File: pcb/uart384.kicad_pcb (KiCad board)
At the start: 2 copper layers, 54.1 x 23.5 mm, 42 parts, among them IC1 ICE40LP384-SG32, J1 USB_A, J2 TC2050, J3 TC2050_ext, J4 Conn_02x07_Odd_Even, SW1 SW_Push, U1 AT25DF256-SSHN, U2 CP2102-QFN28, U3 MIC5365-1.2YC5, U4 AMS1117-2.5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

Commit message: plaster everything with licenses and copyright notices.
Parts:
- added REF**: OSHW-Logo2_7.3x6mm_SilkScreen, Symbol:OSHW-Logo2_7.3x6mm_SilkScreen, F.Cu at (112.9, 75.1)
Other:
- board text added: "CERN-OHL-W v2"
- board text added: "This item was designed by an implementation of RFC2795. Please send fruit to the designer. No bananas."
- board text added: "by dpiegdon"
- board text added: "v2.0~ UART384"
- board text removed: "UART384"
- board text removed: "v2.0~ by dpiegdon"

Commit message: optimize the shit out of the PCB because I'm bored.
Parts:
- JP2: renamed from JP1; footprint Jumper:SolderJumper-3_P1.3mm_Bridged2Bar12_RoundedPad1.0x1.5mm -> Jumper:SolderJumper-3_P1.3mm_Open_RoundedPad1.0x1.5mm
- moved D3 13.3 mm to (101.5, 84.7), turned to -90 degrees
- moved C9 3.11 mm to (105.1, 83.6), turned to -90 degrees
- moved U3 2.34 mm to (107.6, 85.2), turned to 180 degrees
- moved C5 1.91 mm to (107.5, 82.9), turned to 0 degrees
- moved C6 1.90 mm to (104.2, 86.0)
- moved C7 1.89 mm to (98.2, 73.0), turned to 180 degrees
- moved C1 1.68 mm to (99.2, 71.5), turned to 180 degrees
- moved Y1 1.06 mm to (110.8, 84.5)
- moved C13 1.06 mm to (103.4, 83.6), turned to 90 degrees
- moved C4 0.64 mm to (97.2, 74.7), turned to 180 degrees
- renumbered JP2 to JP1
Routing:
- net GND: track 98.3 -> 115.8 mm, vias 7 -> 10
- net +2V5: track 11.1 -> 8.44 mm, vias 2 -> 1
- net +1V2: track 9.04 -> 11.5 mm
- net /CLK: track 7.30 -> 8.01 mm
- net /UART_CTS: track 9.09 -> 8.52 mm
- net +3V3: track 62.5 -> 62.6 mm, vias 20 -> 19

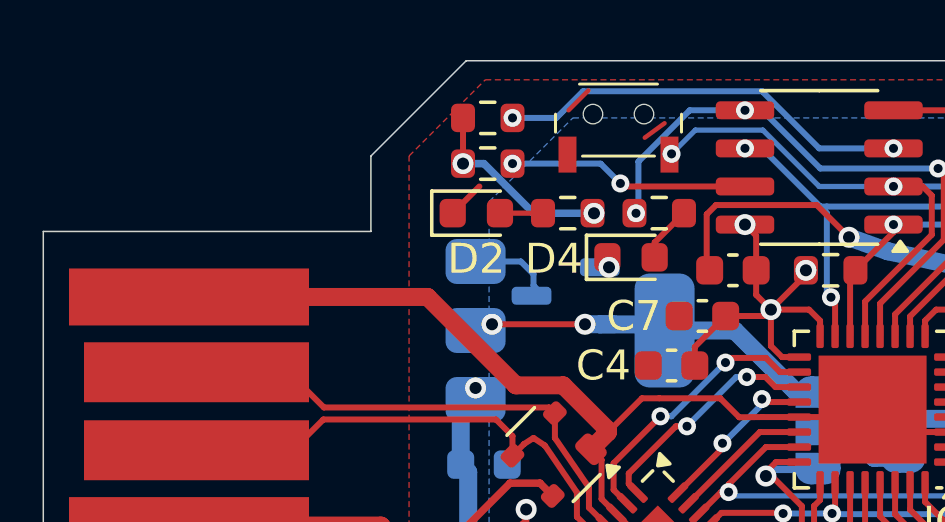
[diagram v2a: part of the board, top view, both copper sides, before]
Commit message: PCB: add in-line resistor to switch SW1 to avoid possible shorts.
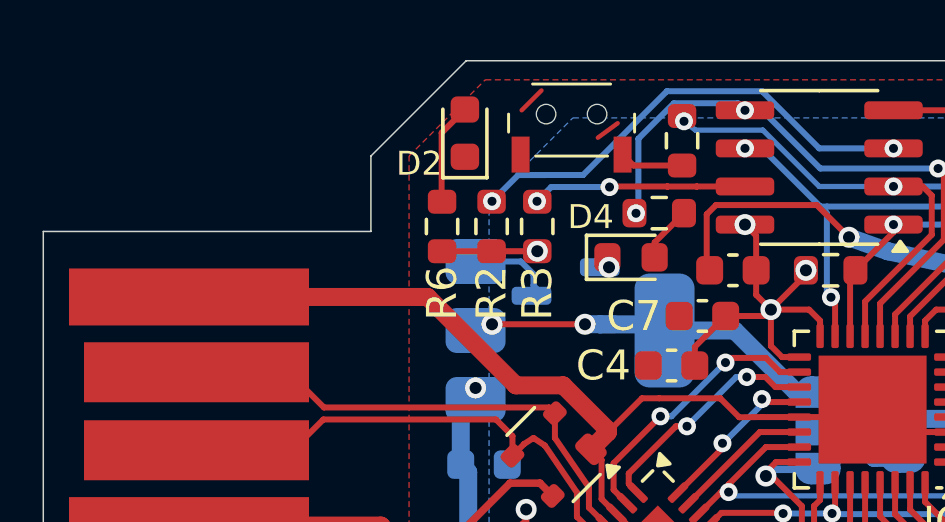
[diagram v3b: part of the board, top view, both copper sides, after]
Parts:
- added R8: 4k7, Resistor_SMD:R_0603_1608Metric, F.Cu at (97.5, 67.2)
- moved R6 4.21 mm to (89.5, 70.0), turned to 90 degrees
- moved R2 3.62 mm to (91.2, 70.0), turned to 90 degrees
- moved D2 2.69 mm to (90.3, 66.9), turned to 90 degrees
- moved R3 2.67 mm to (92.7, 70.0), turned to 90 degrees
- moved SW1 1.56 mm to (93.9, 66.3)
- renumbered R9 to R10, R8 to R9
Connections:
- SW1 pad 2: /SDI -> Net-(R8-Pad2)
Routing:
- net +3V3: track 62.6 -> 59.2 mm, vias 19 -> 18
- net Net-(R8-Pad2): track 0.00 -> 2.13 mm
- net Net-(D2-A): track 1.44 -> 3.40 mm
- net Net-(U1-~{WP}/IO2): track 13.9 -> 15.7 mm
- net GND: track 115.8 -> 114.5 mm
- net Net-(U1-~{HOLD}/IO3): track 8.06 -> 7.16 mm
- net /SDI: track 22.6 -> 21.9 mm
- net /SDO: track 24.1 -> 24.7 mm

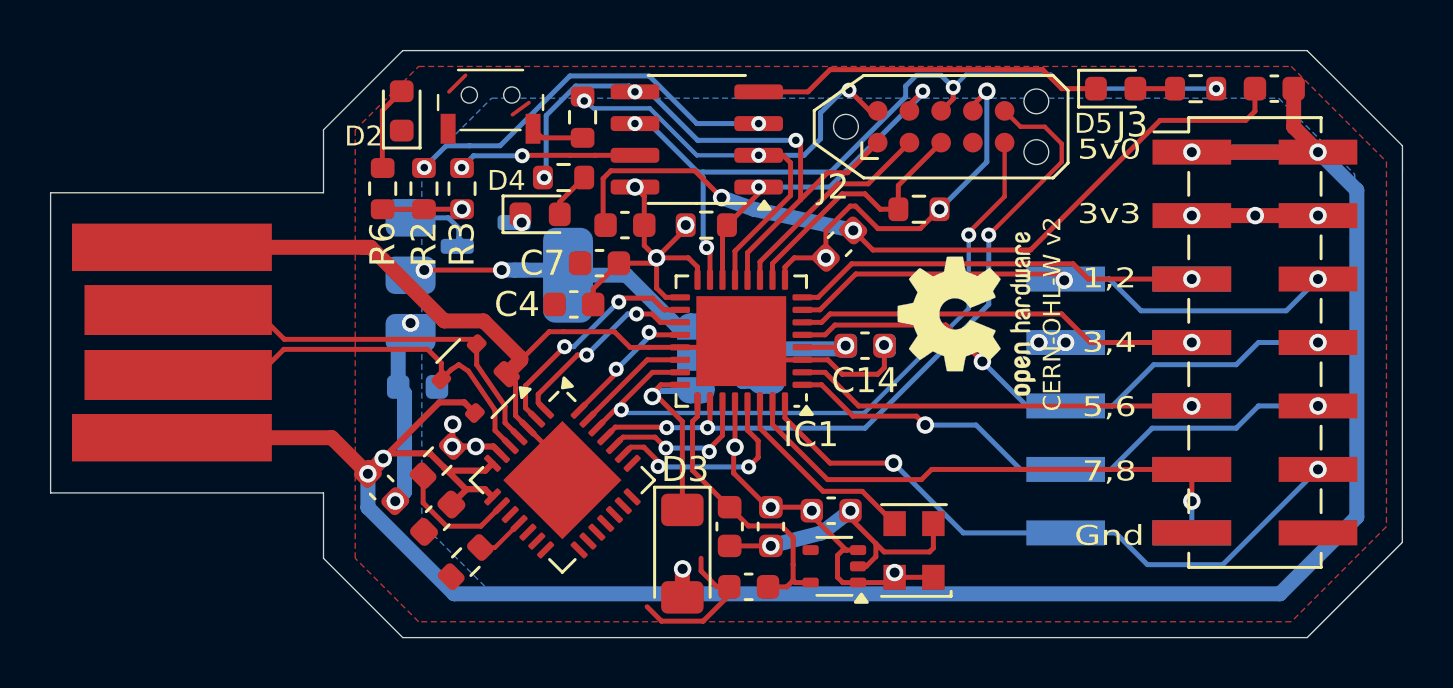
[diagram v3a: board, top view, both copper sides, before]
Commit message: add test-pads for easy access to differential pair GPIO1/GPIO2
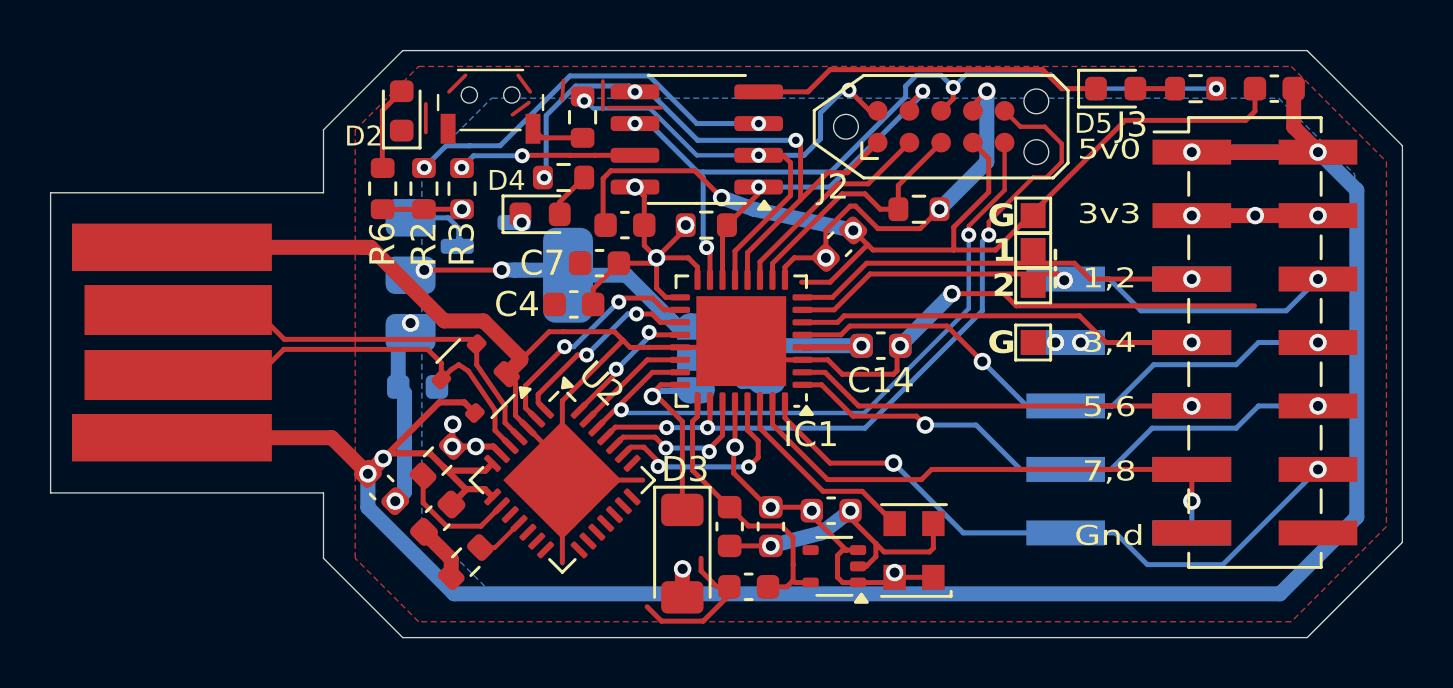
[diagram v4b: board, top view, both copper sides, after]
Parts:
- added TP1: TestPoint, TestPoint:TestPoint_Pad_1.0x1.0mm, F.Cu at (115.6, 72.5)
- added TP2: TestPoint, TestPoint:TestPoint_Pad_1.0x1.0mm, F.Cu at (115.6, 73.9)
- added TP3: TestPoint, TestPoint:TestPoint_Pad_1.0x1.0mm, F.Cu at (115.6, 71.1)
- added TP4: TestPoint, TestPoint:TestPoint_Pad_1.0x1.0mm, F.Cu at (115.6, 76.2)
- REF**: moved to B.Cu
- moved REF** 16.8 mm to (98.0, 82.8)
- moved C14 0.64 mm to (109.5, 76.3)
- moved C12 0.62 mm to (109.5, 76.3)
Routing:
- net GND: track 114.5 -> 160.1 mm, vias 10 -> 11
- net Vdrive: track 4.97 -> 6.24 mm
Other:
- board text added: "1"
- board text added: "2"
- board text added: "G"

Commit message: PCB: add test-pads for easy access to differential pair GPIO5/GPIO6
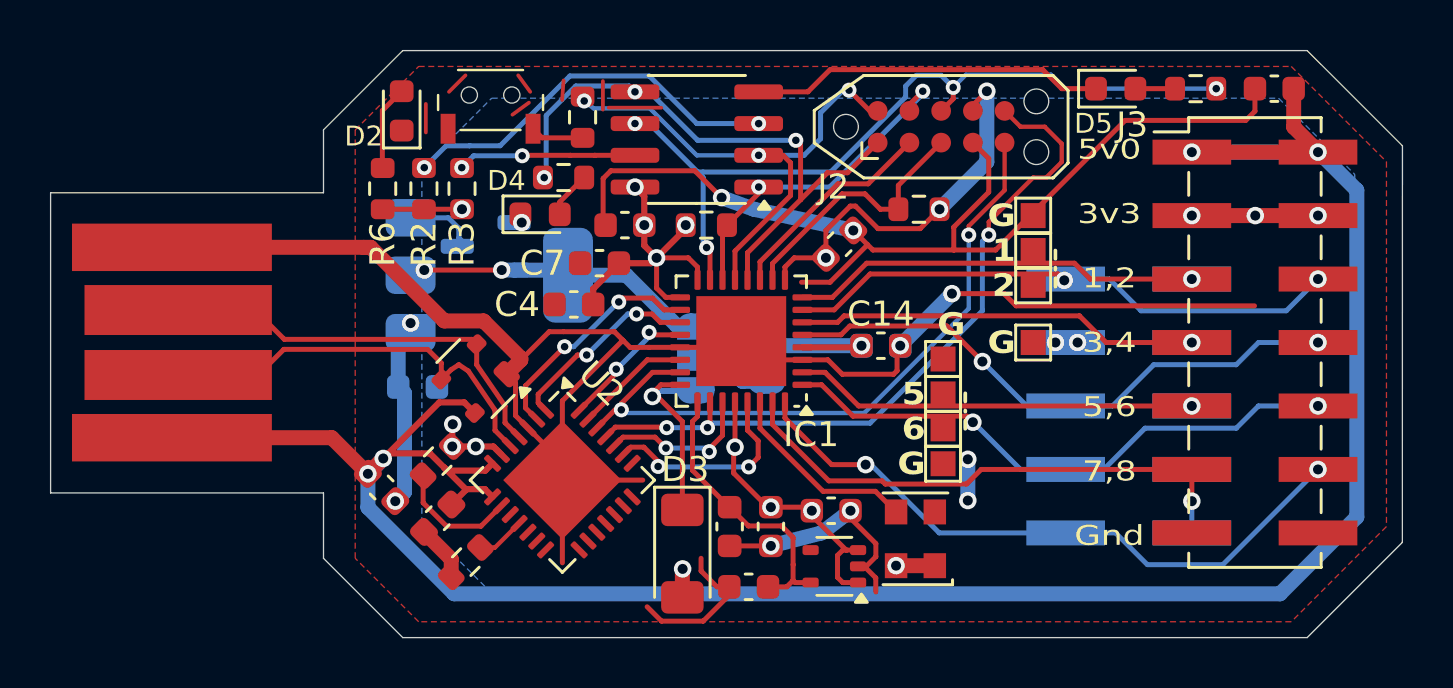
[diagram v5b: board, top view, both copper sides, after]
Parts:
- added TP5: TestPoint, TestPoint:TestPoint_Pad_1.0x1.0mm, F.Cu at (112.0, 78.3)
- added TP6: TestPoint, TestPoint:TestPoint_Pad_1.0x1.0mm, F.Cu at (112.0, 79.7)
- added TP7: TestPoint, TestPoint:TestPoint_Pad_1.0x1.0mm, F.Cu at (112.0, 81.1)
- added TP8: TestPoint, TestPoint:TestPoint_Pad_1.0x1.0mm, F.Cu at (112.0, 76.9)
- moved Y1 0.47 mm to (110.9, 84.1)
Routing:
- net +3V3: track 59.2 -> 57.4 mm, vias 18 -> 19
- net GND: track 160.1 -> 159.6 mm, vias 11 -> 13
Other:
- board text added: "5"
- board text added: "6"

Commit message: release PCB v2.0: production files, schematic
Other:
- board text added: "v2.0 UART384"
- board text removed: "v2.0~ UART384"
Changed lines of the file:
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@@
 	(title_block
 		(title "UART384")
-		(rev "v2.0~dev")
+		(date "2025-10-18")
+		(rev "v2.0")
 		(comment 1 "A USB/UART enabled dev-board for the ice40LP384.")
 		(comment 2 "https://github.com/dpiegdon/uart384")
@@
 			(drillshape 0)
 			(scaleselection 1)
-			(outputdirectory "production/uart384-v1.0/")
+			(outputdirectory "production/uart384-v2.0/")
 		)
 	)
@@
 		)
 	)
-	(gr_text "v2.0~\nUART384"
+	(gr_text "v2.0\nUART384"
 		(at 112.43816 85.217 0)
 		(layer "F.Mask")
